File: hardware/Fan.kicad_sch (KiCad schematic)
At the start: 0 parts

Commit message: added more stuff wip
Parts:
- added C31, C32: 1u, Capacitor_SMD:C_0603_1608Metric, symbol Device:C_Small
- added D14, D15: VSSAF522-M3/H, CustomKiCad-Library:SODFL5226X100N, symbol Diode:C3D25170H
- added FAN1, FAN2: Conn_01x04, Connector_Molex:Molex_Nano-Fit_105309-xx04_1x04_P2.50mm_Vertical, symbol Connector_Generic:Conn_01x04
- added R30, R31: 33k, Resistor_SMD:R_0603_1608Metric, symbol Device:R_US
- added R84, R85: 10k, Resistor_SMD:R_0603_1608Metric, symbol Device:R_US
- added U3: EMC2305-1-AP-TR, CustomKiCad-Library:QFN65P400X400X90-17N-D, symbol 2024-11-02_21-04-42:EMC2305-1-AP-TR
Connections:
- new net +24V: D14.1 (K), D15.1 (K), FAN1.1 (Pin_1), FAN2.1 (Pin_1)
- new net +3.3V: C31.1, C32.1, R30.1, R31.1, R84.1, R85.1, U3.3 (VDD)
- new net ADDRESS_PULLUP: R30.2, U3.4 (ADDR_SEL)
- new net CLK_PULLUP: R31.2, U3.11 (CLK)
- new net FAN_1_PWM: FAN1.3 (Pin_3), U3.5 (PWM1)
- new net FAN_1_TACH: FAN1.2 (Pin_2), R84.2, U3.6 (TACH1)
- new net FAN_2_PWM: FAN2.3 (Pin_3), U3.7 (PWM2)
- new net FAN_2_TACH: FAN2.2 (Pin_2), R85.2, U3.8 (TACH2)
- new net FAN_ALERT: U3.12 (*ALERT)
- new net FAN_SCL: U3.2 (SMCLK)
- new net FAN_SDA: U3.1 (SMDATA)
- new net GND: C31.2, C32.2, D14.2 (A), D15.2 (A), FAN1.4 (Pin_4), FAN2.4 (Pin_4), U3.17 (EPAD)
- no-connect marks 0 -> 6
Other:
- note added: "Configure PWMs as Open Drain"
- note added: "Fan Connectors"
- note added: "Fan Controller"
- note added: "Fan Controller IC"
- note added: "Fig 1-1"
- note added: "Fig 1-2"
- note added: "Important Figures"
- note added: "Over-Voltage Flybacks"

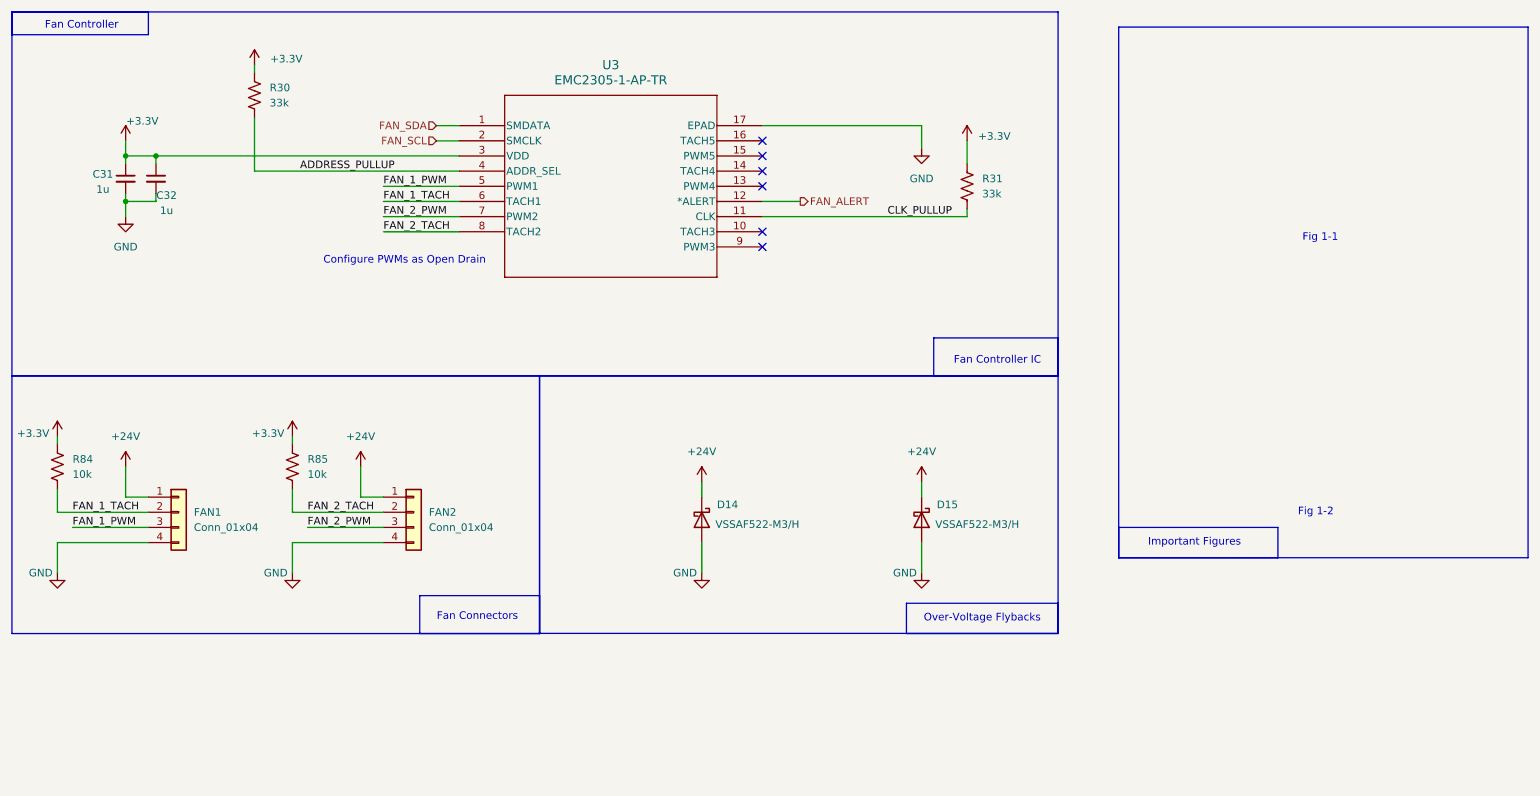
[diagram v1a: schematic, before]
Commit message: some changes - switched to contactor design block - switched to power protection design block - added SD card - added fan I2C pullup - added resistors for ESP32 power mux - shield tied to gnd with 0 ohm - added USB-PD and boost design blocks
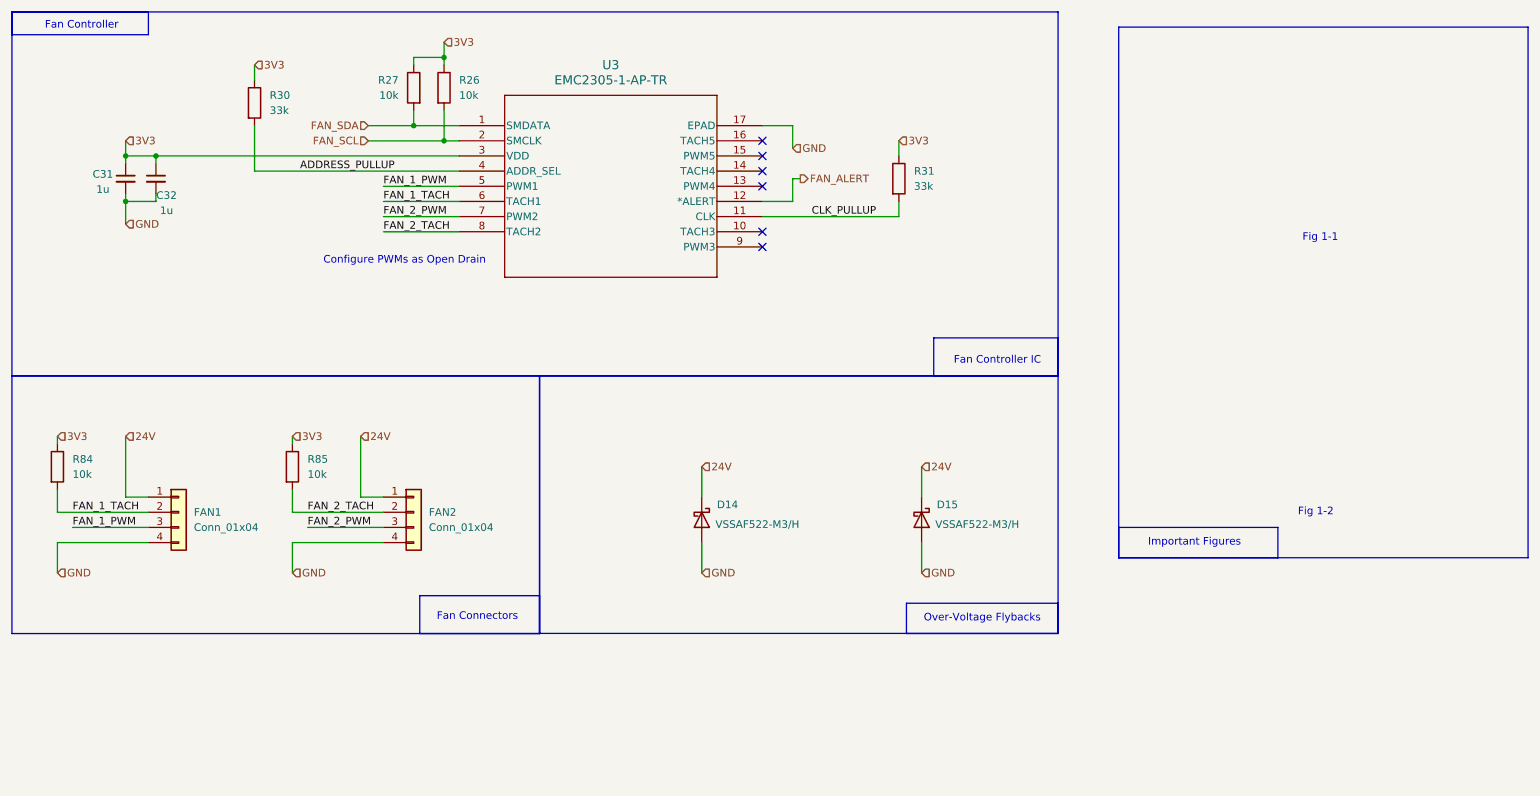
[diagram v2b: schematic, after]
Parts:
- added R26, R27: 10k, Resistor_SMD:R_0603_1608Metric_Pad0.98x0.95mm_HandSolder, symbol Device:R
- R30, R31, R84, R85: symbol Device:R_US -> Device:R
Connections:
- net FAN_SCL: now also R26.2
- net FAN_SDA: now also R27.2
- net +24V renamed 24V
- net +3.3V renamed 3V3
- net 3V3: now also R26.1, R27.1

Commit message: power updates
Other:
- note added: "How many fans?"
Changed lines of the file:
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@@
+		)
+	)
+	(text "How many fans?"
+		(exclude_from_sim no)
+		(at 84.836 145.288 0)
+		(effects
+			(font
+				(size 1.905 1.905)
+				(color 255 0 0 1)
+			)
 		)
 	)

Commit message: finished schematic except for 12v buck boost
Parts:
- C46: renamed from C31; footprint Capacitor_SMD:C_0603_1608Metric -> Capacitor_SMD:C_0603_1608Metric_Pad1.08x0.95mm_HandSolder
- C47: renamed from C32; footprint Capacitor_SMD:C_0603_1608Metric -> Capacitor_SMD:C_0603_1608Metric_Pad1.08x0.95mm_HandSolder
- D19: renamed from D14; footprint CustomKiCad-Library:SODFL5226X100N -> LHRS_Passives:SODFL5226X100N
- D20: renamed from D15; footprint CustomKiCad-Library:SODFL5226X100N -> LHRS_Passives:SODFL5226X100N
- R78: renamed from R84; footprint Resistor_SMD:R_0603_1608Metric -> Resistor_SMD:R_0603_1608Metric_Pad0.98x0.95mm_HandSolder
- R79: renamed from R30; footprint Resistor_SMD:R_0603_1608Metric -> Resistor_SMD:R_0603_1608Metric_Pad0.98x0.95mm_HandSolder
- R80: renamed from R85; footprint Resistor_SMD:R_0603_1608Metric -> Resistor_SMD:R_0603_1608Metric_Pad0.98x0.95mm_HandSolder
- R83: renamed from R31; footprint Resistor_SMD:R_0603_1608Metric -> Resistor_SMD:R_0603_1608Metric_Pad0.98x0.95mm_HandSolder
- U9: renamed from U3; footprint CustomKiCad-Library:QFN65P400X400X90-17N-D -> Package_DFN_QFN:QFN-16-1EP_1.8x2.6mm_P0.4mm_EP0.7x1.5mm
- renumbered R27 to R81, R26 to R82
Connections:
- net 24V renamed 12V
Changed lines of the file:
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@@
 		)
 	)
-	(hierarchical_label "24V"
+	(hierarchical_label "12V"
 		(shape input)
 		(at 133.35 93.98 0)
@@
 		)
 	)
-	(hierarchical_label "24V"
+	(hierarchical_label "12V"
 		(shape input)
 		(at 170.18 93.98 0)
@@
 		)
 	)
-	(hierarchical_label "24V"
+	(hierarchical_label "12V"
 		(shape input)
 		(at 76.2 88.9 0)
@@
 		)
 	)
-	(hierarchical_label "24V"
+	(hierarchical_label "12V"
 		(shape input)
 		(at 36.83 88.9 0)
@@
 		(in_pos_files yes)
 		(dnp no)
-		(property "Reference" "R27"
+		(property "Reference" "R81"
 			(at 82.55 29.2099 0)
 			(show_name no)
@@
 			(project "PS-BPSLeader"
 				(path "/d4a4ed4f-0983-4aef-b212-0e3284ab3963/975a5890-d31b-4bf8-8164-e98394116f83"
-					(reference "R27")
+					(reference "R81")
 					(unit 1)
 				)
@@
 		(in_pos_files yes)
 		(dnp no)
-		(property "Reference" "C32"
+		(property "Reference" "C47"
 			(at 43.688 48.514 0)
 			(show_name no)
@@
 			)
 		)
-		(property "Footprint" "Capacitor_SMD:C_0603_1608Metric"
+		(property "Footprint" "Capacitor_SMD:C_0603_1608Metric_Pad1.08x0.95mm_HandSolder"
 			(at 41.91 45.72 0)
 			(hide yes)
@@
 			(project "PS-BPSLeader"
 				(path "/d4a4ed4f-0983-4aef-b212-0e3284ab3963/975a5890-d31b-4bf8-8164-e98394116f83"
-					(reference "C32")
+					(reference "C47")
 					(unit 1)
 				)
@@
 		(dnp no)
 		(fields_autoplaced yes)
-		(property "Reference" "R30"
+		(property "Reference" "R79"
 			(at 60.96 31.7499 0)
 			(show_name no)
@@
 			)
 		)
-		(property "Footprint" "Resistor_SMD:R_0603_1608Metric"
+		(property "Footprint" "Resistor_SMD:R_0603_1608Metric_Pad0.98x0.95mm_HandSolder"
 			(at 56.642 33.02 90)
 			(hide yes)
@@
 			(project "PS-BPSLeader"
 				(path "/d4a4ed4f-0983-4aef-b212-0e3284ab3963/975a5890-d31b-4bf8-8164-e98394116f83"
-					(reference "R30")
+					(reference "R79")
 					(unit 1)
 				)
@@
 		(in_pos_files yes)
 		(dnp no)
-		(property "Reference" "D14"
+		(property "Reference" "D19"
 			(at 135.89 100.33 90)
 			(show_name no)
@@
 			)
 		)
-		(property "Footprint" "CustomKiCad-Library:SODFL5226X100N"
+		(property "Footprint" "LHRS_Passives:SODFL5226X100N"
 			(at 128.905 102.87 0)
 			(hide yes)
@@
 			(project "PS-BPSLeader"
 				(path "/d4a4ed4f-0983-4aef-b212-0e3284ab3963/975a5890-d31b-4bf8-8164-e98394116f83"
-					(reference "D14")
+					(reference "D19")
 					(unit 1)
 				)
@@
 		(dnp no)
 		(fields_autoplaced yes)
-		(property "Reference" "U3"
+		(property "Reference" "U9"
 			(at 118.11 26.67 0)
 			(show_name no)
@@
 			)
 		)
-		(property "Footprint" "CustomKiCad-Library:QFN65P400X400X90-17N-D"
+		(property "Footprint" "Package_DFN_QFN:QFN-16-1EP_1.8x2.6mm_P0.4mm_EP0.7x1.5mm"
 			(at 92.71 36.83 0)
 			(hide yes)
@@
 			(project "PS-BPSLeader"
 				(path "/d4a4ed4f-0983-4aef-b212-0e3284ab3963/975a5890-d31b-4bf8-8164-e98394116f83"
-					(reference "U3")
+					(reference "U9")
 					(unit 1)
 				)
@@
 		(in_pos_files yes)
 		(dnp no)
-		(property "Reference" "D15"
+		(property "Reference" "D20"
 			(at 172.72 100.33 90)
 			(show_name no)
@@
 			)
 		)
-		(property "Footprint" "CustomKiCad-Library:SODFL5226X100N"
+		(property "Footprint" "LHRS_Passives:SODFL5226X100N"
 			(at 165.735 102.87 0)
 			(hide yes)
@@
 			(project "PS-BPSLeader"
 				(path "/d4a4ed4f-0983-4aef-b212-0e3284ab3963/975a5890-d31b-4bf8-8164-e98394116f83"
-					(reference "D15")
+					(reference "D20")
 					(unit 1)
 				)
@@
 		(dnp no)
 		(fields_autoplaced yes)
-		(property "Reference" "R26"
+		(property "Reference" "R82"
 			(at 92.71 29.2099 0)
 			(show_name no)
@@
 			(project "PS-BPSLeader"
 				(path "/d4a4ed4f-0983-4aef-b212-0e3284ab3963/975a5890-d31b-4bf8-8164-e98394116f83"
-					(reference "R26")
+					(reference "R82")
 					(unit 1)
 				)
@@
 		(dnp no)
 		(fields_autoplaced yes)
-		(property "Reference" "R31"
+		(property "Reference" "R83"
 			(at 168.91 44.4499 0)
 			(show_name no)
@@
 			)
 		)
-		(property "Footprint" "Resistor_SMD:R_0603_1608Metric"
+		(property "Footprint" "Resistor_SMD:R_0603_1608Metric_Pad0.98x0.95mm_HandSolder"
 			(at 164.592 45.72 90)
 			(hide yes)
@@
 			(project "PS-BPSLeader"
 				(path "/d4a4ed4f-0983-4aef-b212-0e3284ab3963/975a5890-d31b-4bf8-8164-e98394116f83"
-					(reference "R31")
+					(reference "R83")
 					(unit 1)
 				)
@@
 		(dnp no)
 		(fields_autoplaced yes)
-		(property "Reference" "R84"
+		(property "Reference" "R78"
 			(at 27.94 92.7099 0)
 			(show_name no)
@@
 			)
 		)
-		(property "Footprint" "Resistor_SMD:R_0603_1608Metric"
+		(property "Footprint" "Resistor_SMD:R_0603_1608Metric_Pad0.98x0.95mm_HandSolder"
 			(at 23.622 93.98 90)
 			(hide yes)
@@
 			(project "PS-BPSLeader"
 				(path "/d4a4ed4f-0983-4aef-b212-0e3284ab3963/975a5890-d31b-4bf8-8164-e98394116f83"
-					(reference "R84")
+					(reference "R78")
 					(unit 1)
 				)
@@
 		(in_pos_files yes)
 		(dnp no)
-		(property "Reference" "C31"
+		(property "Reference" "C46"
 			(at 33.02 44.958 0)
 			(show_name no)
@@
 			)
 		)
-		(property "Footprint" "Capacitor_SMD:C_0603_1608Metric"
+		(property "Footprint" "Capacitor_SMD:C_0603_1608Metric_Pad1.08x0.95mm_HandSolder"
 			(at 36.83 45.72 0)
 			(hide yes)
@@
 			(project "PS-BPSLeader"
 				(path "/d4a4ed4f-0983-4aef-b212-0e3284ab3963/975a5890-d31b-4bf8-8164-e98394116f83"
-					(reference "C31")
+					(reference "C46")
 					(unit 1)
 				)
@@
 		(dnp no)
 		(fields_autoplaced yes)
-		(property "Reference" "R85"
+		(property "Reference" "R80"
 			(at 67.31 92.7099 0)
 			(show_name no)
@@
 			)
 		)
-		(property "Footprint" "Resistor_SMD:R_0603_1608Metric"
+		(property "Footprint" "Resistor_SMD:R_0603_1608Metric_Pad0.98x0.95mm_HandSolder"
 			(at 62.992 93.98 90)
 			(hide yes)
@@
 			(project "PS-BPSLeader"
 				(path "/d4a4ed4f-0983-4aef-b212-0e3284ab3963/975a5890-d31b-4bf8-8164-e98394116f83"
-					(reference "R85")
+					(reference "R80")
 					(unit 1)
 				)

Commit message: added 12V buck boost
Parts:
- renumbered C46 to C47, C47 to C48, D19 to D21, D20 to D22, R78 to R82, R79 to R83, R80 to R84, R81 to R85, R82 to R86, R83 to R87
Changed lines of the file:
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@@
 		(in_pos_files yes)
 		(dnp no)
-		(property "Reference" "R81"
+		(property "Reference" "R85"
 			(at 82.55 29.2099 0)
 			(show_name no)
@@
 			(project "PS-BPSLeader"
 				(path "/d4a4ed4f-0983-4aef-b212-0e3284ab3963/975a5890-d31b-4bf8-8164-e98394116f83"
-					(reference "R81")
+					(reference "R85")
 					(unit 1)
 				)
@@
 		(in_pos_files yes)
 		(dnp no)
-		(property "Reference" "C47"
+		(property "Reference" "C48"
 			(at 43.688 48.514 0)
 			(show_name no)
@@
 			(project "PS-BPSLeader"
 				(path "/d4a4ed4f-0983-4aef-b212-0e3284ab3963/975a5890-d31b-4bf8-8164-e98394116f83"
-					(reference "C47")
+					(reference "C48")
 					(unit 1)
 				)
@@
 		(dnp no)
 		(fields_autoplaced yes)
-		(property "Reference" "R79"
+		(property "Reference" "R83"
 			(at 60.96 31.7499 0)
 			(show_name no)
@@
 			(project "PS-BPSLeader"
 				(path "/d4a4ed4f-0983-4aef-b212-0e3284ab3963/975a5890-d31b-4bf8-8164-e98394116f83"
-					(reference "R79")
+					(reference "R83")
 					(unit 1)
 				)
@@
 		(in_pos_files yes)
 		(dnp no)
-		(property "Reference" "D19"
+		(property "Reference" "D21"
 			(at 135.89 100.33 90)
 			(show_name no)
@@
 			(project "PS-BPSLeader"
 				(path "/d4a4ed4f-0983-4aef-b212-0e3284ab3963/975a5890-d31b-4bf8-8164-e98394116f83"
-					(reference "D19")
+					(reference "D21")
 					(unit 1)
 				)
@@
 		(in_pos_files yes)
 		(dnp no)
-		(property "Reference" "D20"
+		(property "Reference" "D22"
 			(at 172.72 100.33 90)
 			(show_name no)
@@
 			(project "PS-BPSLeader"
 				(path "/d4a4ed4f-0983-4aef-b212-0e3284ab3963/975a5890-d31b-4bf8-8164-e98394116f83"
-					(reference "D20")
+					(reference "D22")
 					(unit 1)
 				)
@@
 		(dnp no)
 		(fields_autoplaced yes)
-		(property "Reference" "R82"
+		(property "Reference" "R86"
 			(at 92.71 29.2099 0)
 			(show_name no)
@@
 			(project "PS-BPSLeader"
 				(path "/d4a4ed4f-0983-4aef-b212-0e3284ab3963/975a5890-d31b-4bf8-8164-e98394116f83"
-					(reference "R82")
+					(reference "R86")
 					(unit 1)
 				)
@@
 		(dnp no)
 		(fields_autoplaced yes)
-		(property "Reference" "R83"
+		(property "Reference" "R87"
 			(at 168.91 44.4499 0)
 			(show_name no)
@@
 			(project "PS-BPSLeader"
 				(path "/d4a4ed4f-0983-4aef-b212-0e3284ab3963/975a5890-d31b-4bf8-8164-e98394116f83"
-					(reference "R83")
+					(reference "R87")
 					(unit 1)
 				)
@@
 		(dnp no)
 		(fields_autoplaced yes)
-		(property "Reference" "R78"
+		(property "Reference" "R82"
 			(at 27.94 92.7099 0)
 			(show_name no)
@@
 			(project "PS-BPSLeader"
 				(path "/d4a4ed4f-0983-4aef-b212-0e3284ab3963/975a5890-d31b-4bf8-8164-e98394116f83"
-					(reference "R78")
+					(reference "R82")
 					(unit 1)
 				)
@@
 		(in_pos_files yes)
 		(dnp no)
-		(property "Reference" "C46"
+		(property "Reference" "C47"
 			(at 33.02 44.958 0)
 			(show_name no)
@@
 			(project "PS-BPSLeader"
 				(path "/d4a4ed4f-0983-4aef-b212-0e3284ab3963/975a5890-d31b-4bf8-8164-e98394116f83"
-					(reference "C46")
+					(reference "C47")
 					(unit 1)
 				)
@@
 		(dnp no)
 		(fields_autoplaced yes)
-		(property "Reference" "R80"
+		(property "Reference" "R84"
 			(at 67.31 92.7099 0)
 			(show_name no)
@@
 			(project "PS-BPSLeader"
 				(path "/d4a4ed4f-0983-4aef-b212-0e3284ab3963/975a5890-d31b-4bf8-8164-e98394116f83"
-					(reference "R80")
+					(reference "R84")
 					(unit 1)
 				)
